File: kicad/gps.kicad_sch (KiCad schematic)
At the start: 37 parts, among them CN1 SMA-KWE_C7498154, J7 SMA-KWE_C7498154, U12 MAX-M10S-00B, U13 74LVC1G17SE-7, U14 74LVC1G17SE-7

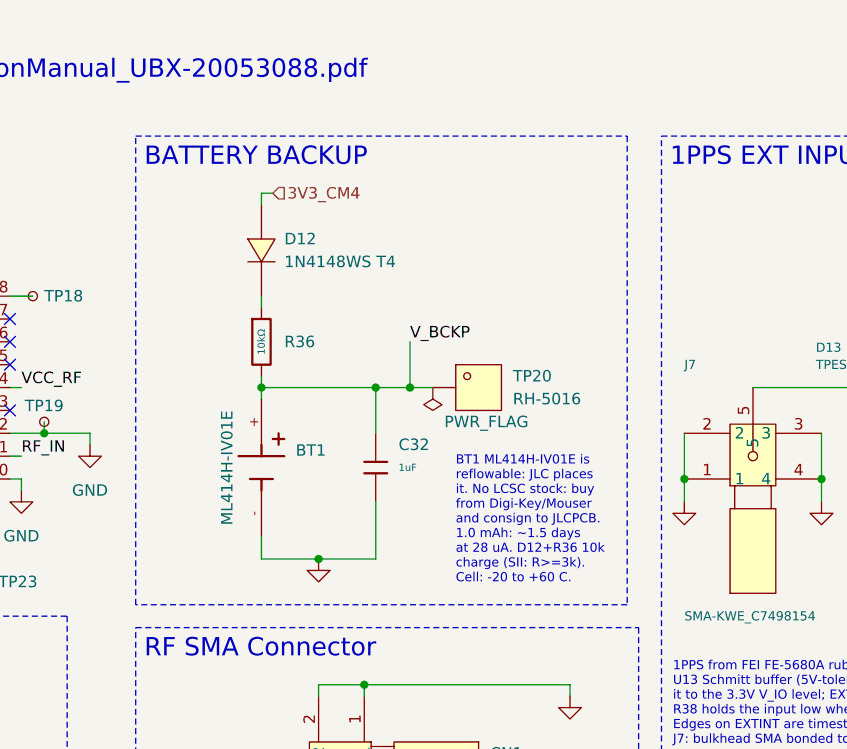
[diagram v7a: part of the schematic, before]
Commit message: Updates after latest Tomachie review
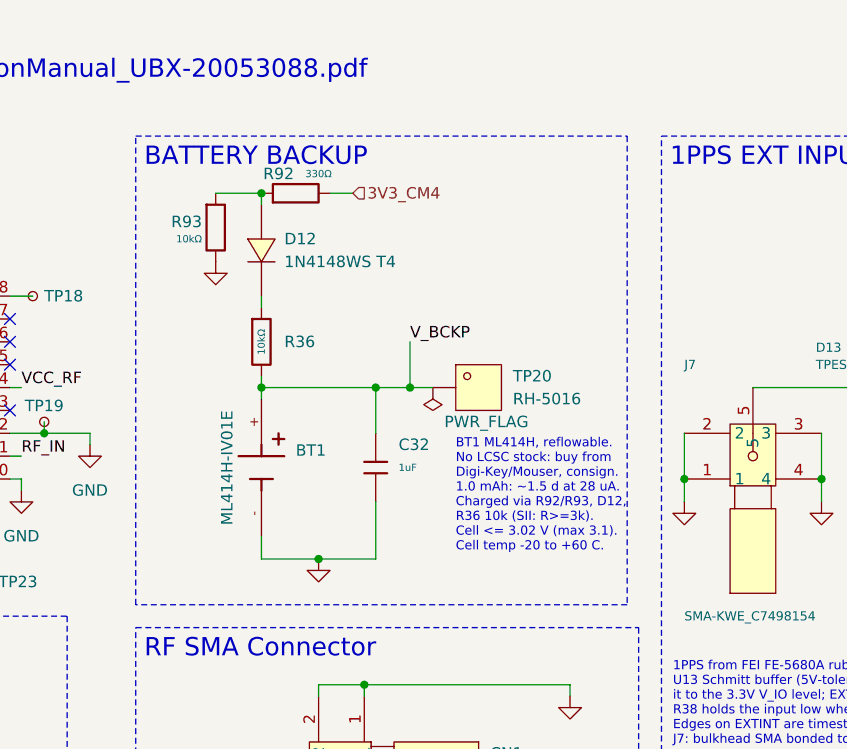
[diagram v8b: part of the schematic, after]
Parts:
- added R92: 330Ω, MyPartsIPC:RESC1608X55N, symbol MyParts:0603WAF3300T5E
- added R93: 10kΩ, MyPartsIPC:RESC1608X55N, symbol MyParts:0603WAF1002T5E
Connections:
- net 3V3_CM4: now also R92.2; no longer D12.2 (A)
- net GND: now also R93.2
- new net: D12.2 (A), R92.1, R93.1
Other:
- note added: "BT1 ML414H, reflowable. No LCSC stock: buy from Digi-Key/Mouser, consign. 1.0 mAh: ~1.5 d at 28 uA. Charged via R92/R93, D12, R36 10k (SII: R>=3k). Cell <= 3.02 V (max 3.1). Cell temp -20 to +60 C."
- note removed: "BT1 ML414H-IV01E is reflowable: JLC places it. No LCSC stock: buy from Digi-Key/Mouser and consign to JLCPCB. 1.0 mAh: ~1.5 days at 28 uA. D12+R36 10k charge (SII: R>=3k). Cell: -20 to +60 C."
